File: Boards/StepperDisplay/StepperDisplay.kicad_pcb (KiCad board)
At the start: 2 copper layers, 99.8 x 99.8 mm, 106 parts, among them IC1 ATTINY861-P, P1 CONN_01X06, P2 ISP, Q1 BC817-40, Q10 BC817-40, Q11 BC817-40, Q12 BC817-40, Q13 BC817-40, Q14 BC817-40, Q15 BC817-40, Q16 BC817-40, Q17 BC817-40, Q18 BC817-40, Q19 BC817-40, Q2 BC817-40, Q3 BC817-40, Q4 BC817-40, Q5 BC817-40, Q6 BC817-40, Q7 BC817-40, Q8 BC817-40, Q9 BC817-40, SW1 SW_PUSH, U1 74HC595, U2 74HC595, U3 ULN2801A, U4 74HC595, U5 74HC595, U6 ULN2801A, U7 74HC595, U8 74HC595, U9 ULN2801A, X1 12MHz

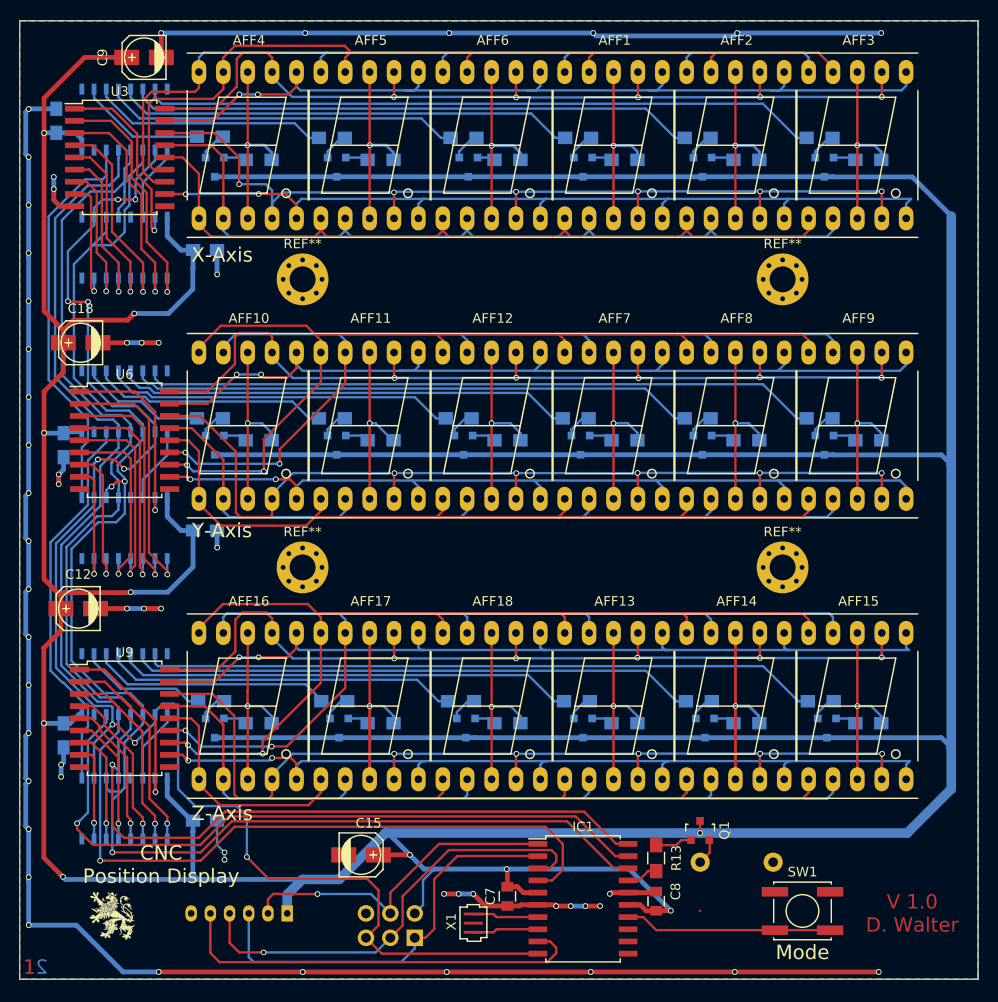
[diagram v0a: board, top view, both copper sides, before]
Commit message: New LED Driving Scheme
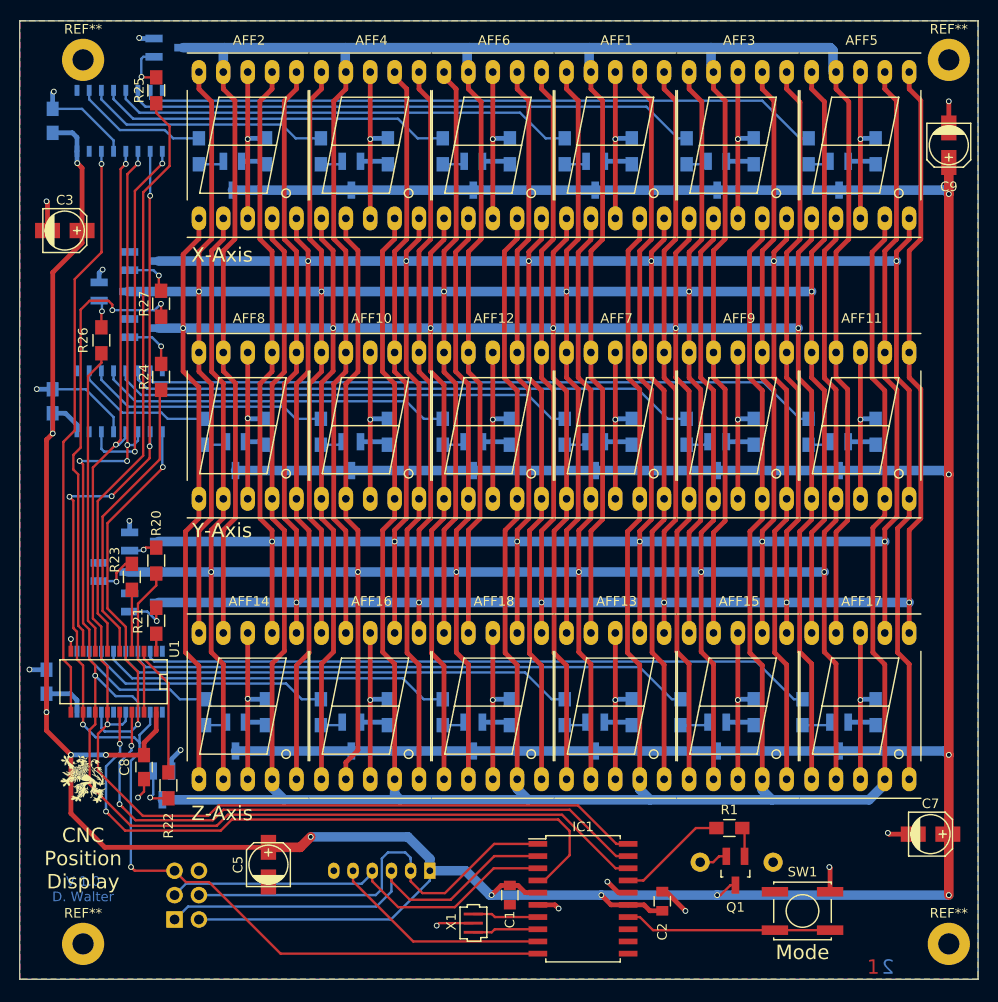
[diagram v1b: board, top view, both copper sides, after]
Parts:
- removed C11, C13, C14, C16, C17: 100nF, Capacitors_SMD:C_0805_HandSoldering
- removed C12, C15, C18: 100µF, Capacitors_SMD:c_elec_4x5.8
- removed the REF** at (96.5, 98.6)
- removed the REF** at (146.5, 98.6)
- removed the REF** at (96.5, 68.6)
- removed the REF** at (146.5, 68.6)
- removed U5, U7, U8: 74HC595, SMD_Packages:SO-16-N
- removed U6, U9: ULN2801A, Housings_SOIC:SOIC-18_7.5x11.6mm_Pitch1.27mm
- added C1: 100nF, Capacitors_SMD:C_0805, F.Cu at (118.1, 132.7)
- added C2: 100nF, Capacitors_SMD:C_0805, F.Cu at (134.0, 133.3)
- added C3: 100µF, Capacitors_SMD:c_elec_4x5.8, F.Cu at (71.8, 63.5)
- added C4: 100nF, Capacitors_SMD:C_0805_HandSoldering, B.Cu at (70.5, 81.3)
- added C5: 100µF, Capacitors_SMD:c_elec_4x5.8, F.Cu at (93.0, 129.5)
- added C6: 100nF, Capacitors_SMD:C_0805_HandSoldering, B.Cu at (70.5, 52.1)
- added Q20: BC817-40, TO_SOT_Packages_SMD:SOT-23_Handsoldering, B.Cu at (139.7, 87.0)
- added Q21: BC817-40, TO_SOT_Packages_SMD:SOT-23_Handsoldering, B.Cu at (152.4, 87.0)
- added Q22: BC817-40, TO_SOT_Packages_SMD:SOT-23_Handsoldering, B.Cu at (89.5, 116.2)
- added Q23: BC817-40, TO_SOT_Packages_SMD:SOT-23_Handsoldering, B.Cu at (101.6, 116.2)
- added Q24: BC817-40, TO_SOT_Packages_SMD:SOT-23_Handsoldering, B.Cu at (114.3, 116.2)
- added Q25: BC817-40, TO_SOT_Packages_SMD:SOT-23_Handsoldering, B.Cu at (127.0, 116.2)
- added Q26: BC817-40, TO_SOT_Packages_SMD:SOT-23_Handsoldering, B.Cu at (139.7, 116.2)
- added Q27: BC817-40, TO_SOT_Packages_SMD:SOT-23_Handsoldering, B.Cu at (152.4, 116.2)
- added R14: 18R, Resistors_SMD:R_0805_HandSoldering, B.Cu at (130.8, 113.7)
- added R27: 100R, Resistors_SMD:R_0805_HandSoldering, F.Cu at (81.8, 71.1)
- added R28: 1k, Resistors_SMD:R_0805_HandSoldering, B.Cu at (85.7, 55.2)
- added R41: 1k, Resistors_SMD:R_0805_HandSoldering, B.Cu at (98.4, 113.7)
- added R42: 1k, Resistors_SMD:R_0805_HandSoldering, B.Cu at (111.1, 113.7)
- added R43: 1k, Resistors_SMD:R_0805_HandSoldering, B.Cu at (123.8, 113.7)
- added R44: 1k, Resistors_SMD:R_0805_HandSoldering, B.Cu at (135.9, 113.7)
- added R45: 1k, Resistors_SMD:R_0805_HandSoldering, B.Cu at (148.6, 113.7)
- added REF**: MountingHole_2.2mm_M2_Pad, Mounting_Holes:MountingHole_2.2mm_M2_Pad, F.Cu at (163.8, 45.7)
- added REF**: MountingHole_2.2mm_M2_Pad, Mounting_Holes:MountingHole_2.2mm_M2_Pad, F.Cu at (73.7, 45.7)
- added REF**: MountingHole_2.2mm_M2_Pad, Mounting_Holes:MountingHole_2.2mm_M2_Pad, F.Cu at (73.7, 137.8)
- added REF**: MountingHole_2.2mm_M2_Pad, Mounting_Holes:MountingHole_2.2mm_M2_Pad, F.Cu at (163.8, 137.8)
- C7: value 100nF -> 100µF; footprint Capacitors_SMD:C_0805 -> Capacitors_SMD:c_elec_4x5.8
- C8: footprint Capacitors_SMD:C_0805 -> Capacitors_SMD:C_0805_HandSoldering
- P1: value CONN_01X06 -> ISP; footprint w_conn_jst-ph:b6b-ph-kl -> Pin_Headers:Pin_Header_Straight_2x03
- P2: value ISP -> CONN_01X06; footprint Pin_Headers:Pin_Header_Straight_2x03 -> w_conn_jst-ph:b6b-ph-kl
- Q1, Q10, Q11, Q12, Q13, Q14, Q15, Q16, Q17, Q18, Q19: footprint TO_SOT_Packages_SMD:SOT-23 -> TO_SOT_Packages_SMD:SOT-23_Handsoldering
- Q2, Q3, Q4, Q5, Q6, Q7, Q8, Q9: value BC817-40 -> IRLML2502; footprint TO_SOT_Packages_SMD:SOT-23 -> TO_SOT_Packages_SMD:SOT-23_Handsoldering
- R1, U1: moved to F.Cu
- R13: value 1k -> 18R; moved to B.Cu
- R15, R16, R17, R18, R19, R2, R3, R4, R5, R6: value 1k -> 18R
- R20: value 1k -> 100R; moved to F.Cu
- R21, R22, R23, R24, R25, R26: value 18R -> 100R; moved to F.Cu
- R35, R36, R37, R38, R39, R40: value 18R -> 1k
- U3: value ULN2801A -> 74HC595; footprint Housings_SOIC:SOIC-18_7.5x11.6mm_Pitch1.27mm -> SMD_Packages:SO-16-N; moved to B.Cu
- moved R1 90.1 mm to (141.0, 125.7)
- moved C9 84.3 mm to (163.8, 54.6), turned to 270 degrees
- moved R26 80.6 mm to (75.6, 74.9), turned to 270 degrees
- moved Q14 77.8 mm to (139.7, 57.8)
- moved Q15 77.6 mm to (152.4, 57.8)
- moved Q4 71.8 mm to (81.9, 121.3)
- moved R25 71.5 mm to (81.3, 48.9), turned to 270 degrees
- moved R20 70.7 mm to (81.3, 97.9), turned to 270 degrees
- moved R34 70.0 mm to (86.4, 84.5), turned to 90 degrees
- moved Q7 69.5 mm to (82.5, 44.5), turned to 90 degrees
- moved R40 69.1 mm to (86.4, 113.7), turned to 90 degrees
- moved Q5 64.6 mm to (76.8, 99.1), turned to 90 degrees
- moved Q6 60.5 mm to (80.0, 73.7), turned to 90 degrees
- moved U1 58.6 mm to (76.8, 110.5), turned to 180 degrees
- moved R29 58.4 mm to (98.4, 55.2), turned to 90 degrees
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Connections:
- net Net-(U1-Pad9) renamed /LEDS/LEDsX/Ser_In
- AFF1 pad 1: Net-(AFF1-Pad1) -> Seg5
- AFF1 pad 10: Net-(AFF1-Pad10) -> Seg7
- AFF1 pad 2: Net-(AFF1-Pad2) -> Seg4
- AFF1 pad 4: Net-(AFF1-Pad4) -> Seg3
- AFF1 pad 5: Net-(AFF1-Pad5) -> Seg8
- AFF1 pad 6: Net-(AFF1-Pad6) -> Seg2
- AFF1 pad 7: Net-(AFF1-Pad7) -> Seg1
- AFF1 pad 9: Net-(AFF1-Pad9) -> Seg6
- AFF10 pad 1: Net-(AFF10-Pad1) -> Seg5
- AFF10 pad 10: Net-(AFF10-Pad10) -> Seg7
- AFF10 pad 2: Net-(AFF10-Pad2) -> Seg4
- AFF10 pad 4: Net-(AFF10-Pad4) -> Seg3
- AFF10 pad 5: Net-(AFF10-Pad5) -> Seg8
- AFF10 pad 6: Net-(AFF10-Pad6) -> Seg2
- AFF10 pad 7: Net-(AFF10-Pad7) -> Seg1
- AFF10 pad 9: Net-(AFF10-Pad9) -> Seg6
- AFF11 pad 1: Net-(AFF10-Pad1) -> Seg5
- AFF11 pad 10: Net-(AFF10-Pad10) -> Seg7
- AFF11 pad 2: Net-(AFF10-Pad2) -> Seg4
- AFF11 pad 4: Net-(AFF10-Pad4) -> Seg3
- AFF11 pad 5: Net-(AFF10-Pad5) -> Seg8
- AFF11 pad 6: Net-(AFF10-Pad6) -> Seg2
- AFF11 pad 7: Net-(AFF10-Pad7) -> Seg1
- AFF11 pad 9: Net-(AFF10-Pad9) -> Seg6
- AFF12 pad 1: Net-(AFF10-Pad1) -> Seg5
- AFF12 pad 10: Net-(AFF10-Pad10) -> Seg7
- AFF12 pad 2: Net-(AFF10-Pad2) -> Seg4
- AFF12 pad 4: Net-(AFF10-Pad4) -> Seg3
- AFF12 pad 5: Net-(AFF10-Pad5) -> Seg8
- AFF12 pad 6: Net-(AFF10-Pad6) -> Seg2
- AFF12 pad 7: Net-(AFF10-Pad7) -> Seg1
- AFF12 pad 9: Net-(AFF10-Pad9) -> Seg6
- AFF13 pad 1: Net-(AFF13-Pad1) -> Seg5
- AFF13 pad 10: Net-(AFF13-Pad10) -> Seg7
- AFF13 pad 2: Net-(AFF13-Pad2) -> Seg4
- AFF13 pad 4: Net-(AFF13-Pad4) -> Seg3
- AFF13 pad 5: Net-(AFF13-Pad5) -> Seg8
- AFF13 pad 6: Net-(AFF13-Pad6) -> Seg2
- AFF13 pad 7: Net-(AFF13-Pad7) -> Seg1
- AFF13 pad 9: Net-(AFF13-Pad9) -> Seg6
- AFF14 pad 1: Net-(AFF13-Pad1) -> Seg5
- AFF14 pad 10: Net-(AFF13-Pad10) -> Seg7
- AFF14 pad 2: Net-(AFF13-Pad2) -> Seg4
- AFF14 pad 4: Net-(AFF13-Pad4) -> Seg3
- AFF14 pad 5: Net-(AFF13-Pad5) -> Seg8
- AFF14 pad 6: Net-(AFF13-Pad6) -> Seg2
- AFF14 pad 7: Net-(AFF13-Pad7) -> Seg1
- AFF14 pad 9: Net-(AFF13-Pad9) -> Seg6
- AFF15 pad 1: Net-(AFF13-Pad1) -> Seg5
- AFF15 pad 10: Net-(AFF13-Pad10) -> Seg7
- AFF15 pad 2: Net-(AFF13-Pad2) -> Seg4
- AFF15 pad 4: Net-(AFF13-Pad4) -> Seg3
- AFF15 pad 5: Net-(AFF13-Pad5) -> Seg8
- AFF15 pad 6: Net-(AFF13-Pad6) -> Seg2
- AFF15 pad 7: Net-(AFF13-Pad7) -> Seg1
- AFF15 pad 9: Net-(AFF13-Pad9) -> Seg6
- AFF16 pad 1: Net-(AFF13-Pad1) -> Seg5
- AFF16 pad 10: Net-(AFF13-Pad10) -> Seg7
- AFF16 pad 2: Net-(AFF13-Pad2) -> Seg4
- AFF16 pad 4: Net-(AFF13-Pad4) -> Seg3
- AFF16 pad 5: Net-(AFF13-Pad5) -> Seg8
- AFF16 pad 6: Net-(AFF13-Pad6) -> Seg2
- AFF16 pad 7: Net-(AFF13-Pad7) -> Seg1
- AFF16 pad 9: Net-(AFF13-Pad9) -> Seg6
- AFF17 pad 1: Net-(AFF13-Pad1) -> Seg5
- AFF17 pad 10: Net-(AFF13-Pad10) -> Seg7
- AFF17 pad 2: Net-(AFF13-Pad2) -> Seg4
- AFF17 pad 4: Net-(AFF13-Pad4) -> Seg3
- AFF17 pad 5: Net-(AFF13-Pad5) -> Seg8
- AFF17 pad 6: Net-(AFF13-Pad6) -> Seg2
- AFF17 pad 7: Net-(AFF13-Pad7) -> Seg1
- AFF17 pad 9: Net-(AFF13-Pad9) -> Seg6
- AFF18 pad 1: Net-(AFF13-Pad1) -> Seg5
- AFF18 pad 10: Net-(AFF13-Pad10) -> Seg7
- AFF18 pad 2: Net-(AFF13-Pad2) -> Seg4
- AFF18 pad 4: Net-(AFF13-Pad4) -> Seg3
- AFF18 pad 5: Net-(AFF13-Pad5) -> Seg8
- AFF18 pad 6: Net-(AFF13-Pad6) -> Seg2
- AFF18 pad 7: Net-(AFF13-Pad7) -> Seg1
- AFF18 pad 9: Net-(AFF13-Pad9) -> Seg6
- AFF2 pad 1: Net-(AFF1-Pad1) -> Seg5
- AFF2 pad 10: Net-(AFF1-Pad10) -> Seg7
- AFF2 pad 2: Net-(AFF1-Pad2) -> Seg4
- AFF2 pad 4: Net-(AFF1-Pad4) -> Seg3
- AFF2 pad 5: Net-(AFF1-Pad5) -> Seg8
- AFF2 pad 6: Net-(AFF1-Pad6) -> Seg2
- AFF2 pad 7: Net-(AFF1-Pad7) -> Seg1
- AFF2 pad 9: Net-(AFF1-Pad9) -> Seg6
- AFF3 pad 1: Net-(AFF1-Pad1) -> Seg5
- AFF3 pad 10: Net-(AFF1-Pad10) -> Seg7
- AFF3 pad 2: Net-(AFF1-Pad2) -> Seg4
- AFF3 pad 4: Net-(AFF1-Pad4) -> Seg3
- AFF3 pad 5: Net-(AFF1-Pad5) -> Seg8
- AFF3 pad 6: Net-(AFF1-Pad6) -> Seg2
- AFF3 pad 7: Net-(AFF1-Pad7) -> Seg1
- AFF3 pad 9: Net-(AFF1-Pad9) -> Seg6
- AFF4 pad 1: Net-(AFF1-Pad1) -> Seg5
- AFF4 pad 10: Net-(AFF1-Pad10) -> Seg7
- AFF4 pad 2: Net-(AFF1-Pad2) -> Seg4
- AFF4 pad 4: Net-(AFF1-Pad4) -> Seg3
- AFF4 pad 5: Net-(AFF1-Pad5) -> Seg8
- AFF4 pad 6: Net-(AFF1-Pad6) -> Seg2
- AFF4 pad 7: Net-(AFF1-Pad7) -> Seg1
- AFF4 pad 9: Net-(AFF1-Pad9) -> Seg6
- AFF5 pad 1: Net-(AFF1-Pad1) -> Seg5
- AFF5 pad 10: Net-(AFF1-Pad10) -> Seg7
- AFF5 pad 2: Net-(AFF1-Pad2) -> Seg4
- AFF5 pad 4: Net-(AFF1-Pad4) -> Seg3
- AFF5 pad 5: Net-(AFF1-Pad5) -> Seg8
- AFF5 pad 6: Net-(AFF1-Pad6) -> Seg2
- AFF5 pad 7: Net-(AFF1-Pad7) -> Seg1
- AFF5 pad 9: Net-(AFF1-Pad9) -> Seg6
- AFF6 pad 1: Net-(AFF1-Pad1) -> Seg5
- AFF6 pad 10: Net-(AFF1-Pad10) -> Seg7
- AFF6 pad 2: Net-(AFF1-Pad2) -> Seg4
- AFF6 pad 4: Net-(AFF1-Pad4) -> Seg3
- AFF6 pad 5: Net-(AFF1-Pad5) -> Seg8
- AFF6 pad 6: Net-(AFF1-Pad6) -> Seg2
- AFF6 pad 7: Net-(AFF1-Pad7) -> Seg1
- AFF6 pad 9: Net-(AFF1-Pad9) -> Seg6
- AFF7 pad 1: Net-(AFF10-Pad1) -> Seg5
- AFF7 pad 10: Net-(AFF10-Pad10) -> Seg7
- AFF7 pad 2: Net-(AFF10-Pad2) -> Seg4
- AFF7 pad 4: Net-(AFF10-Pad4) -> Seg3
- AFF7 pad 5: Net-(AFF10-Pad5) -> Seg8
- AFF7 pad 6: Net-(AFF10-Pad6) -> Seg2
- AFF7 pad 7: Net-(AFF10-Pad7) -> Seg1
- AFF7 pad 9: Net-(AFF10-Pad9) -> Seg6
- AFF8 pad 1: Net-(AFF10-Pad1) -> Seg5
- AFF8 pad 10: Net-(AFF10-Pad10) -> Seg7
- AFF8 pad 2: Net-(AFF10-Pad2) -> Seg4
- AFF8 pad 4: Net-(AFF10-Pad4) -> Seg3
- AFF8 pad 5: Net-(AFF10-Pad5) -> Seg8
- AFF8 pad 6: Net-(AFF10-Pad6) -> Seg2
- AFF8 pad 7: Net-(AFF10-Pad7) -> Seg1
- AFF8 pad 9: Net-(AFF10-Pad9) -> Seg6
- AFF9 pad 1: Net-(AFF10-Pad1) -> Seg5
- AFF9 pad 10: Net-(AFF10-Pad10) -> Seg7
- AFF9 pad 2: Net-(AFF10-Pad2) -> Seg4
- AFF9 pad 4: Net-(AFF10-Pad4) -> Seg3
- AFF9 pad 5: Net-(AFF10-Pad5) -> Seg8
- AFF9 pad 6: Net-(AFF10-Pad6) -> Seg2
- AFF9 pad 7: Net-(AFF10-Pad7) -> Seg1
- AFF9 pad 9: Net-(AFF10-Pad9) -> Seg6
- IC1 pad 19: /LEDsZ/Ser_In -> /LEDS/Ser_In
- P1 pad 1: +5V -> Net-(IC1-Pad2)
- P1 pad 2: Net-(IC1-Pad1) -> +5V
- P1 pad 3: Net-(IC1-Pad2) -> Net-(IC1-Pad3)
- P1 pad 4: Net-(IC1-Pad3) -> Net-(IC1-Pad1)
- P1 pad 5: Net-(IC1-Pad9) -> /Controller/Reset
- P2 pad 1: Net-(IC1-Pad2) -> +5V
- P2 pad 2: +5V -> Net-(IC1-Pad1)
- P2 pad 3: Net-(IC1-Pad3) -> Net-(IC1-Pad2)
- P2 pad 4: Net-(IC1-Pad1) -> Net-(IC1-Pad3)
- P2 pad 5: /Controller/Reset -> Net-(IC1-Pad9)
- Q2 pad 2: Net-(Q2-Pad2) -> GND
- Q2 pad 3: +5V -> Seg1
- Q3 pad 2: Net-(Q3-Pad2) -> GND
- Q3 pad 3: +5V -> Seg2
- Q4 pad 2: Net-(Q4-Pad2) -> GND
- Q4 pad 3: +5V -> Seg3
- Q5 pad 2: Net-(Q5-Pad2) -> GND
- Q5 pad 3: +5V -> Seg4
- Q6 pad 2: Net-(Q6-Pad2) -> GND
- Q6 pad 3: +5V -> Seg5
- Q7 pad 2: Net-(Q7-Pad2) -> GND
- Q7 pad 3: +5V -> Seg6
- Q8 pad 2: Net-(Q8-Pad2) -> GND
- Q8 pad 3: +5V -> Seg7
- Q9 pad 2: Net-(Q9-Pad2) -> GND
- Q9 pad 3: +5V -> Seg8
- R1 pad 1: Net-(Q2-Pad1) -> Net-(Q1-Pad1)
- R1 pad 2: Net-(R1-Pad2) -> Net-(IC1-Pad17)
- R10 pad 1: Net-(Q5-Pad2) -> Net-(Q20-Pad2)
- R10 pad 2: Net-(AFF1-Pad3) -> Net-(AFF9-Pad3)
- R11 pad 1: Net-(Q6-Pad2) -> Net-(Q17-Pad2)
- R11 pad 2: Net-(AFF2-Pad3) -> Net-(AFF10-Pad3)
- R12 pad 1: Net-(Q7-Pad2) -> Net-(Q21-Pad2)
- R12 pad 2: Net-(AFF3-Pad3) -> Net-(AFF11-Pad3)
- R13 pad 1: Net-(Q1-Pad1) -> Net-(Q18-Pad2)
- R13 pad 2: Net-(IC1-Pad17) -> Net-(AFF12-Pad3)
- R15 pad 1: Net-(Q8-Pad1) -> Net-(Q22-Pad2)
- R15 pad 2: Net-(R15-Pad2) -> Net-(AFF14-Pad3)
- R16 pad 1: Net-(Q9-Pad1) -> Net-(Q26-Pad2)
- R16 pad 2: Net-(R16-Pad2) -> Net-(AFF15-Pad3)
- R17 pad 1: Net-(Q10-Pad1) -> Net-(Q23-Pad2)
- R17 pad 2: Net-(R17-Pad2) -> Net-(AFF16-Pad3)
- R18 pad 1: Net-(Q11-Pad1) -> Net-(Q27-Pad2)
- R18 pad 2: Net-(R18-Pad2) -> Net-(AFF17-Pad3)
- R19 pad 1: Net-(Q12-Pad1) -> Net-(Q24-Pad2)
- R19 pad 2: Net-(R19-Pad2) -> Net-(AFF18-Pad3)
- R2 pad 1: Net-(Q3-Pad1) -> Net-(Q13-Pad2)
- R2 pad 2: Net-(R2-Pad2) -> Net-(AFF1-Pad3)
- R20 pad 1: Net-(Q13-Pad1) -> Net-(Q2-Pad1)
- R20 pad 2: Net-(R20-Pad2) -> /LEDS/Q1
- R21 pad 1: Net-(Q8-Pad2) -> Net-(Q3-Pad1)
- R21 pad 2: Net-(AFF10-Pad3) -> /LEDS/Q2
- R22 pad 1: Net-(Q9-Pad2) -> Net-(Q4-Pad1)
- R22 pad 2: Net-(AFF11-Pad3) -> /LEDS/Q3
- R23 pad 1: Net-(Q10-Pad2) -> Net-(Q5-Pad1)
- R23 pad 2: Net-(AFF12-Pad3) -> /LEDS/Q4
- R24 pad 1: Net-(Q11-Pad2) -> Net-(Q6-Pad1)
- R24 pad 2: Net-(AFF7-Pad3) -> /LEDS/Q5
- R25 pad 1: Net-(Q12-Pad2) -> Net-(Q7-Pad1)
- R25 pad 2: Net-(AFF8-Pad3) -> /LEDS/Q6
- R26 pad 1: Net-(Q13-Pad2) -> Net-(Q8-Pad1)
- R26 pad 2: Net-(AFF9-Pad3) -> /LEDS/Q7
- R29 pad 1: Net-(Q14-Pad1) -> Net-(Q11-Pad1)
- R3 pad 1: Net-(Q4-Pad1) -> Net-(Q10-Pad2)
- R3 pad 2: Net-(R3-Pad2) -> Net-(AFF2-Pad3)
- R30 pad 1: Net-(Q15-Pad1) -> Net-(Q12-Pad1)
- R31 pad 1: Net-(Q16-Pad1) -> Net-(Q13-Pad1)
- R32 pad 1: Net-(Q17-Pad1) -> Net-(Q14-Pad1)
- R33 pad 1: Net-(Q18-Pad1) -> Net-(Q15-Pad1)
- R34 pad 1: Net-(Q19-Pad1) -> Net-(Q16-Pad1)
- R35 pad 1: Net-(Q14-Pad2) -> Net-(Q17-Pad1)
- R35 pad 2: Net-(AFF16-Pad3) -> Net-(R35-Pad2)
- R36 pad 1: Net-(Q15-Pad2) -> Net-(Q18-Pad1)
- R36 pad 2: Net-(AFF17-Pad3) -> Net-(R36-Pad2)
- R37 pad 1: Net-(Q16-Pad2) -> Net-(Q19-Pad1)
- R37 pad 2: Net-(AFF18-Pad3) -> Net-(R37-Pad2)
- R38 pad 1: Net-(Q17-Pad2) -> Net-(Q20-Pad1)
- R38 pad 2: Net-(AFF13-Pad3) -> Net-(R38-Pad2)
- R39 pad 1: Net-(Q18-Pad2) -> Net-(Q21-Pad1)
- R39 pad 2: Net-(AFF14-Pad3) -> Net-(R39-Pad2)
- R4 pad 1: Net-(Q5-Pad1) -> Net-(Q14-Pad2)
- R4 pad 2: Net-(R4-Pad2) -> Net-(AFF3-Pad3)
- R40 pad 1: Net-(Q19-Pad2) -> Net-(Q22-Pad1)
- R40 pad 2: Net-(AFF15-Pad3) -> Net-(R40-Pad2)
- R5 pad 1: Net-(Q6-Pad1) -> Net-(Q11-Pad2)
- R5 pad 2: Net-(R5-Pad2) -> Net-(AFF4-Pad3)
- R6 pad 1: Net-(Q7-Pad1) -> Net-(Q15-Pad2)
- R6 pad 2: Net-(R6-Pad2) -> Net-(AFF5-Pad3)
- R7 pad 1: Net-(Q2-Pad2) -> Net-(Q12-Pad2)
- R7 pad 2: Net-(AFF4-Pad3) -> Net-(AFF6-Pad3)
- R8 pad 1: Net-(Q3-Pad2) -> Net-(Q19-Pad2)
- R8 pad 2: Net-(AFF5-Pad3) -> Net-(AFF7-Pad3)
- R9 pad 1: Net-(Q4-Pad2) -> Net-(Q16-Pad2)
- R9 pad 2: Net-(AFF6-Pad3) -> Net-(AFF8-Pad3)
- U1 pad 1: (no net) -> /LEDS/Q2
- U1 pad 14: /LEDsX/Ser_In -> /LEDS/Ser_In
- U1 pad 15: (no net) -> /LEDS/Q1
- U1 pad 2: Net-(R1-Pad2) -> /LEDS/Q3
- U1 pad 3: Net-(R2-Pad2) -> /LEDS/Q4
- U1 pad 4: Net-(R3-Pad2) -> /LEDS/Q5
- U1 pad 5: Net-(R4-Pad2) -> /LEDS/Q6
- U1 pad 6: Net-(R5-Pad2) -> /LEDS/Q7
- U1 pad 7: Net-(R6-Pad2) -> /LEDS/Q8
- U2 pad 1: Net-(U2-Pad1) -> (no net)
- U2 pad 15: Net-(U2-Pad15) -> (no net)
- U2 pad 2: Net-(U2-Pad2) -> Net-(R28-Pad2)
- U2 pad 3: Net-(U2-Pad3) -> Net-(R29-Pad2)
- U2 pad 4: Net-(U2-Pad4) -> Net-(R30-Pad2)
- U2 pad 5: Net-(U2-Pad5) -> Net-(R31-Pad2)
- U2 pad 6: Net-(U2-Pad6) -> Net-(R32-Pad2)
- U2 pad 7: Net-(U2-Pad7) -> Net-(R33-Pad2)
- U2 pad 9: (no net) -> /LEDS/LEDsY/Ser_In
- U3 pad 1: Net-(U2-Pad15) -> (no net)
- U3 pad 10: (no net) -> /Controller/Reset
- U3 pad 11: Net-(AFF1-Pad5) -> /Controller/Ser_Clock
- U3 pad 12: Net-(AFF1-Pad10) -> /Controller/R_Clock
- U3 pad 13: Net-(AFF1-Pad9) -> GND
- U3 pad 14: Net-(AFF1-Pad1) -> /LEDS/LEDsY/Ser_In
- U3 pad 15: Net-(AFF1-Pad2) -> (no net)
- U3 pad 16: Net-(AFF1-Pad4) -> +5V
- U3 pad 2: Net-(U2-Pad1) -> Net-(R34-Pad2)
- U3 pad 3: Net-(U2-Pad2) -> Net-(R35-Pad2)
- U3 pad 4: Net-(U2-Pad3) -> Net-(R36-Pad2)
- U3 pad 5: Net-(U2-Pad4) -> Net-(R37-Pad2)
- U3 pad 6: Net-(U2-Pad5) -> Net-(R38-Pad2)
- U3 pad 7: Net-(U2-Pad6) -> Net-(R39-Pad2)
- U3 pad 8: Net-(U2-Pad7) -> GND
- U3 pad 9: GND -> /LEDS/LEDsZ/Ser_In
- U4 pad 13: /Controller/Enable -> GND
- U4 pad 14: /LEDsY/Ser_In -> /LEDS/LEDsZ/Ser_In
- U4 pad 2: Net-(R15-Pad2) -> Net-(R40-Pad2)
- U4 pad 3: Net-(R16-Pad2) -> Net-(R41-Pad2)
- U4 pad 4: Net-(R17-Pad2) -> Net-(R42-Pad2)
- U4 pad 5: Net-(R18-Pad2) -> Net-(R43-Pad2)
- U4 pad 6: Net-(R19-Pad2) -> Net-(R44-Pad2)
- U4 pad 7: Net-(R20-Pad2) -> Net-(R45-Pad2)
- U4 pad 9: Net-(U4-Pad9) -> (no net)
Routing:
- net Seg3: track 0.00 -> 455.0 mm
- net Seg6: track 0.00 -> 448.3 mm
- net Seg2: track 0.00 -> 442.0 mm, vias 0 -> 6
- net Seg1: track 0.00 -> 440.4 mm, vias 0 -> 6
- net Seg8: track 0.00 -> 440.1 mm, vias 0 -> 6
- net Seg4: track 0.00 -> 437.2 mm, vias 0 -> 6
- net Seg7: track 0.00 -> 436.8 mm, vias 0 -> 6
- net Seg5: track 0.00 -> 431.1 mm, vias 0 -> 6
- net GND: track 312.3 -> 56.8 mm, vias 54 -> 17
- net Net-(AFF13-Pad9): track 104.5 -> 0.00 mm, vias 2 -> 0
- net Net-(AFF13-Pad4): track 103.6 -> 0.00 mm, vias 5 -> 0
- net Net-(AFF10-Pad9): track 101.2 -> 0.00 mm, vias 2 -> 0
- net Net-(AFF13-Pad10): track 101.2 -> 0.00 mm, vias 2 -> 0
- net Net-(AFF10-Pad10): track 100.4 -> 0.00 mm, vias 2 -> 0
- net Net-(AFF10-Pad4): track 98.9 -> 0.00 mm, vias 5 -> 0
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
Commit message: Minor Layout changes
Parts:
- added REF***: OSHW-Logo_5.7x6mm_SilkScreen, Symbols:OSHW-Logo_5.7x6mm_SilkScreen, F.Cu at (104.8, 137.8)
- SW1: footprint Buttons_Switches_SMD:SW_SPST_EVPBF -> SMD_Switch_LSX1301:SW_LSx_1301
- moved G*** 83.9 mm to (139.7, 68.8)
- moved SW1 5.80 mm to (154.3, 133.3)
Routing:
- net Net-(IC1-Pad14): track 21.6 -> 28.7 mm
- net Net-(Q3-Pad1): track 4.63 -> 6.92 mm
- net /LEDS/Q8: track 47.4 -> 49.0 mm
- net GND: track 56.8 -> 55.6 mm, vias 17 -> 16
- net /Controller/Enable: track 68.0 -> 68.5 mm
